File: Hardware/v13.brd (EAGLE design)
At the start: 50 x 50 mm, 86 parts, among them J1 22-27-2081-08, J2 22-27-2031-03

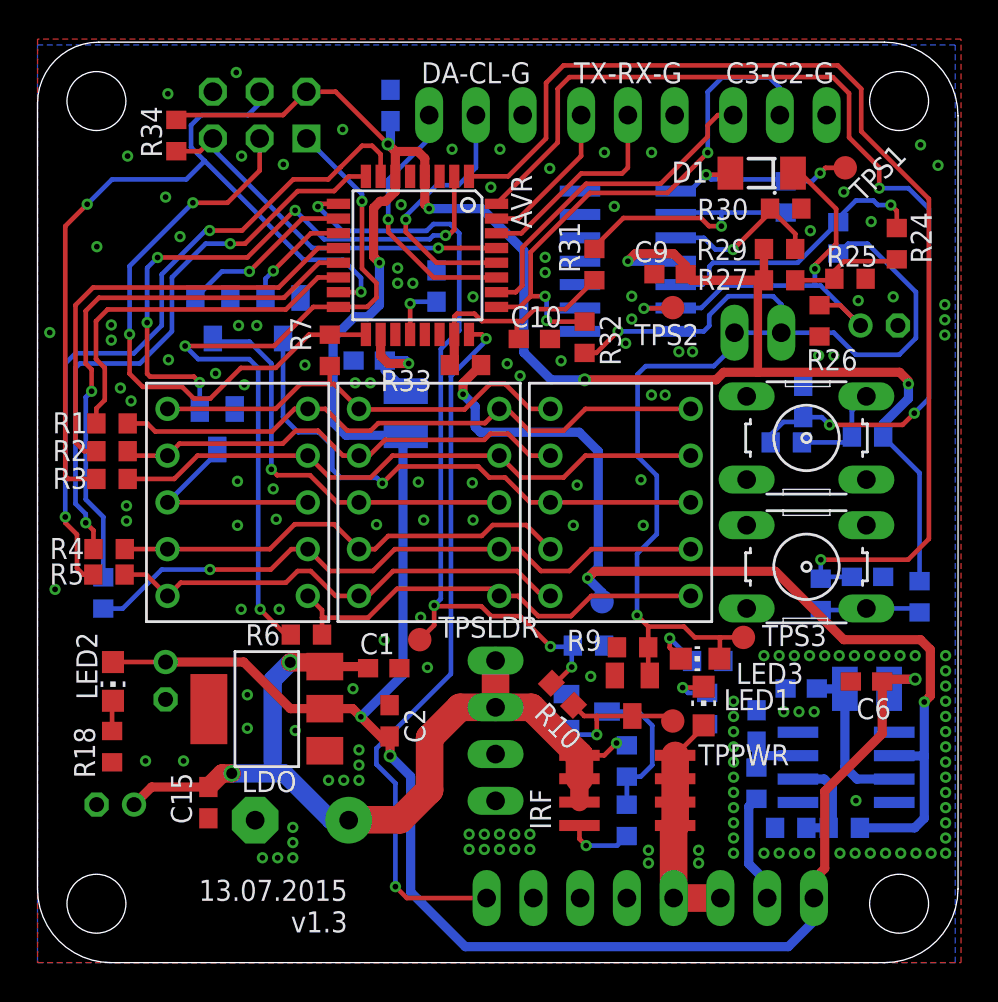
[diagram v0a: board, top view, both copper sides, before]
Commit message: added 5v pin header for twi added optional pull-ups for twi moved some parts around and rerouted some wires
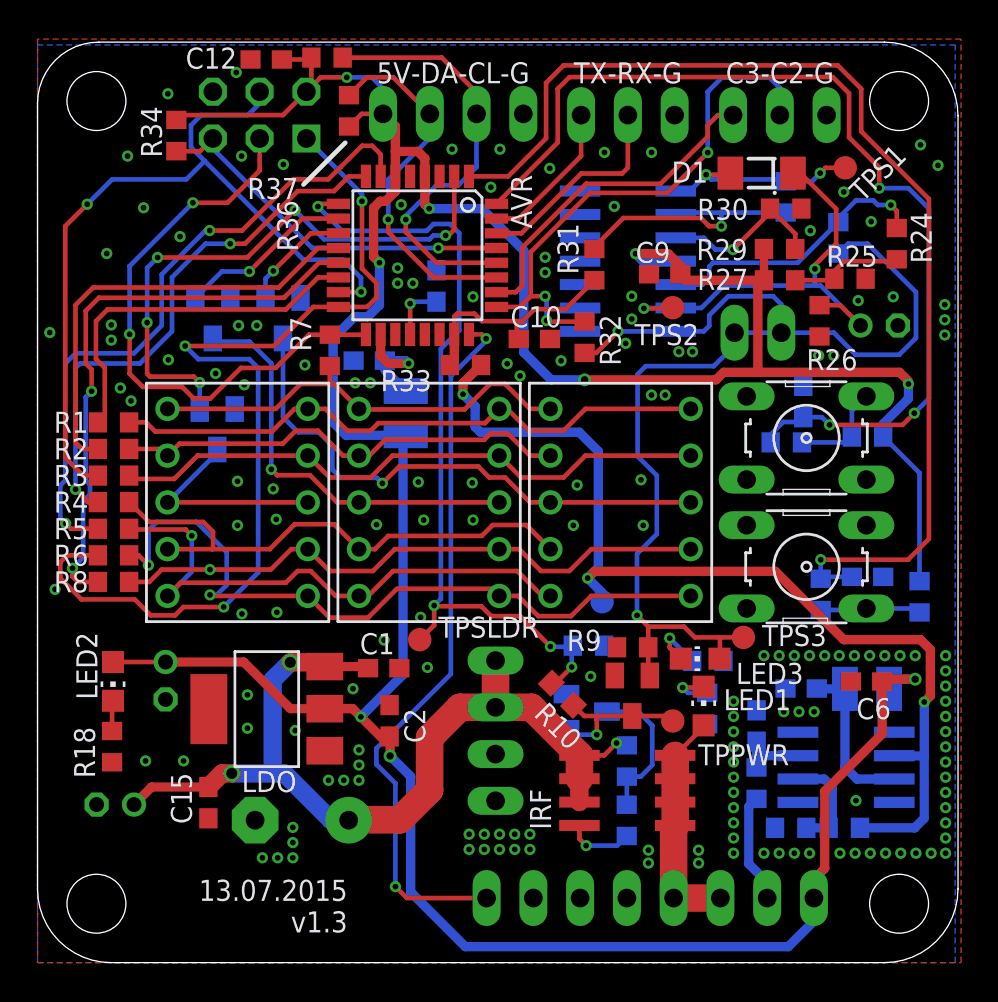
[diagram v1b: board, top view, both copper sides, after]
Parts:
- added R36, R37: 4k7, rcl:R0603
- I2C: value 22-27-2031-03 -> 22-27-2041-04; device con-molex:6410-03 -> con-molex:6410-04
- R25: value 6.2k -> 6k2
- moved R6 11.3 mm to (4.13, 22.1)
- moved C12 7.20 mm to (12.4, 49.1), flipped to the top, turned to 180 degrees
- moved R4 2.56 mm to (4.13, 25.0)
- moved R5 2.50 mm to (4.13, 23.6)
- moved I2C 1.24 mm to (22.6, 46.1)
- moved R8 0.82 mm to (4.13, 20.7), flipped to the top, turned to 180 degrees
- moved C9 0.29 mm to (34.1, 37.4)
- moved R3 0.20 mm to (4.13, 26.5)
- moved R2 0.14 mm to (4.13, 27.9)
- moved R1 0.10 mm to (4.13, 29.3)
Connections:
- net GND: now also I2C.4; no longer I2C.3
- net SCL: now also I2C.3, R37.1; no longer I2C.2
- net SDA: now also I2C.2, R36.1; no longer I2C.1
- net VCC: now also I2C.1, R36.2, R37.2
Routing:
- net N$31: track 24.2 -> 39.6 mm, vias 0 -> 2
- net MISO: track 41.6 -> 52.9 mm
- net SCL: track 14.2 -> 23.5 mm
- net VCC: track 188.4 -> 194.3 mm
- net SDA: track 14.2 -> 19.9 mm
- net N$37: track 25.9 -> 30.4 mm, vias 0 -> 1
- net N$36: track 25.3 -> 29.2 mm
- net LCD_E: track 32.0 -> 29.9 mm
- net N$38: track 35.2 -> 33.2 mm
- net LCD_D: track 37.5 -> 35.8 mm
- net LCD_C: track 29.9 -> 31.5 mm, vias 1 -> 2
- net MOSI: track 44.6 -> 44.0 mm
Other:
- board text added: "5V-DA-CL-G"
- board text removed: "DA-CL-G"

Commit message: [hardware] Adds A4 frame to schematic, Signalnames
and changed name of signal of pwm output to PWM_OUT
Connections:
- net N$33 renamed PWM_OUT
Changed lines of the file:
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@@
 <?xml version="1.0" encoding="utf-8"?>
 <!DOCTYPE eagle SYSTEM "eagle.dtd">
-<eagle version="7.2.0">
+<eagle version="7.3.0">
 <drawing>
 <settings>
@@
 <wire x1="32.013525" y1="8.587475" x2="32.004" y2="8.57795" width="0.254" layer="16"/>
 </signal>
-<signal name="N$33">
+<signal name="PWM_OUT">
 <contactref element="IRF" pad="8"/>
 <contactref element="IRF" pad="7"/>

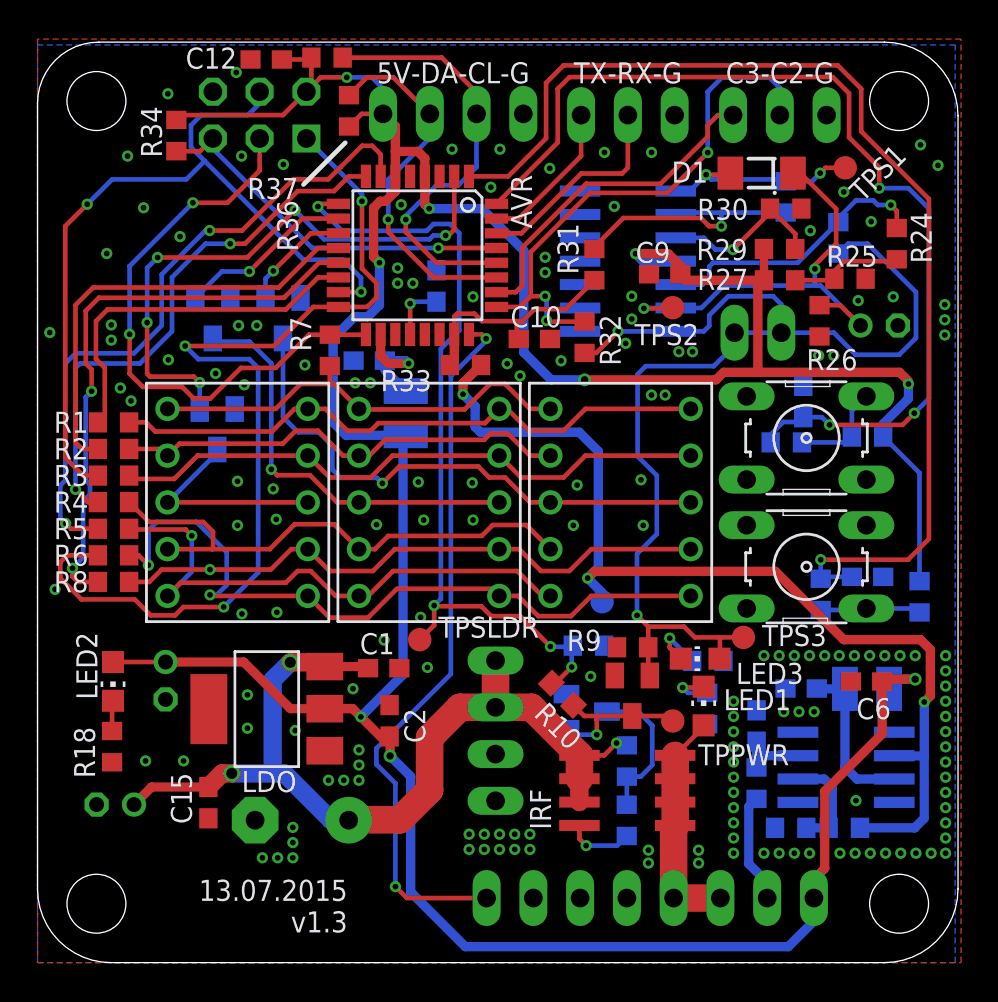
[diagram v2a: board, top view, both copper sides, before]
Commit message: changed radius of round corners changed location of the drilling holes slightly cleared some space around the drilling holes added 2x 10k to set all unused LM324 inputs to a 2,5V moved some components around
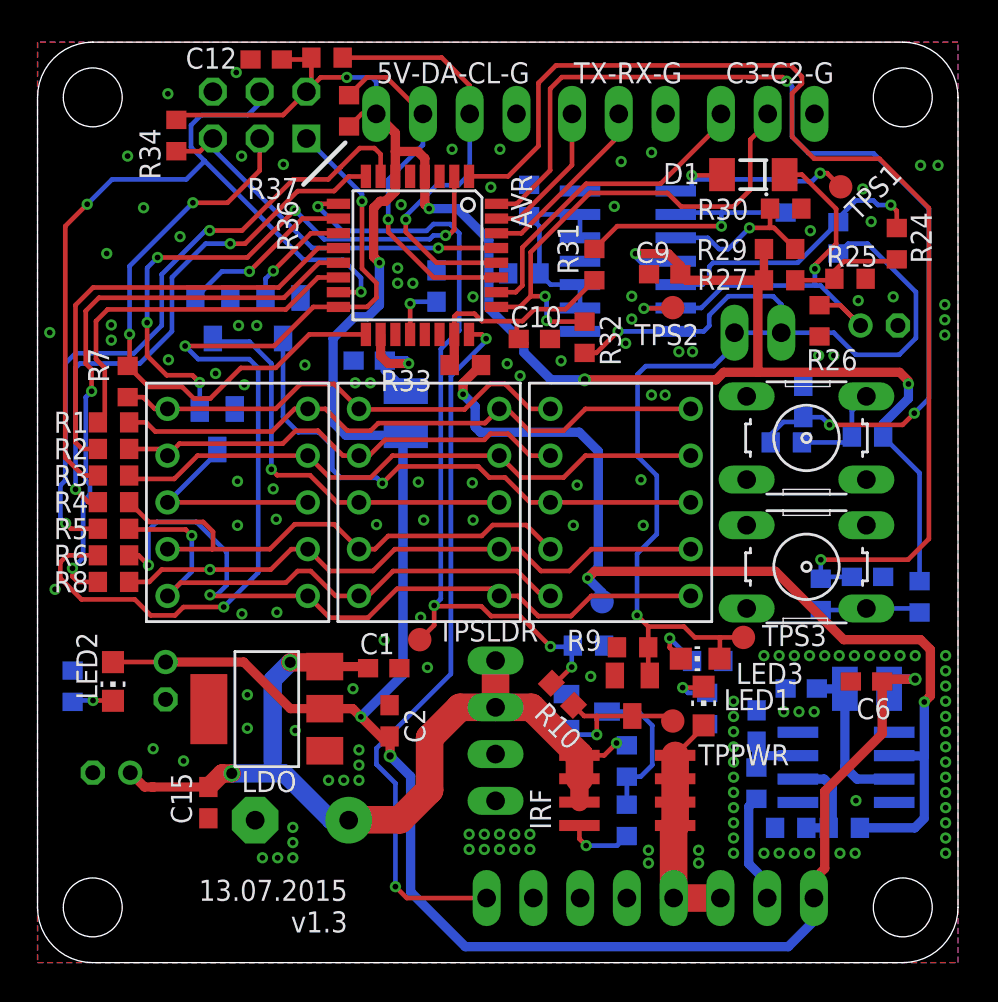
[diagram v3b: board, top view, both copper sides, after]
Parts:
- added R39, R40: 10k, rcl:R0603
- moved R7 11.1 mm to (4.90, 31.6)
- moved R18 3.92 mm to (1.91, 15.0), flipped to the bottom, turned to 270 degrees
- moved C14 1.75 mm to (4.02, 10.3)
- moved TPS1 1.06 mm to (43.6, 42.1)
- moved J2 0.66 mm to (39.7, 46.1)
- moved UART 0.50 mm to (31.6, 46.1)
- moved D1 0.46 mm to (38.9, 42.8)
- moved I2C 0.37 mm to (22.2, 46.1)
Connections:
- new net N$4: LM324.10, LM324.12, LM324.13, LM324.9, R39.2, R40.1
- net GND: now also R40.2
- net VCC: now also R39.1
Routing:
- net N$4: track 0.00 -> 11.1 mm
- net PC2: track 30.3 -> 27.6 mm, vias 3 -> 2
- net RX: track 11.5 -> 10.0 mm
- net N$35: track 24.1 -> 25.5 mm
- net BUTTON_+: track 61.2 -> 62.4 mm
- net PC3: track 18.4 -> 17.7 mm
- net N$7: track 11.4 -> 12.0 mm
- net N$24: track 1.66 -> 2.23 mm, vias 0 -> 1
- net SDA: track 19.9 -> 19.3 mm
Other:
- outline, holes or cut-outs redrawn

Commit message: changed arrangement of parts to be almost all vertical
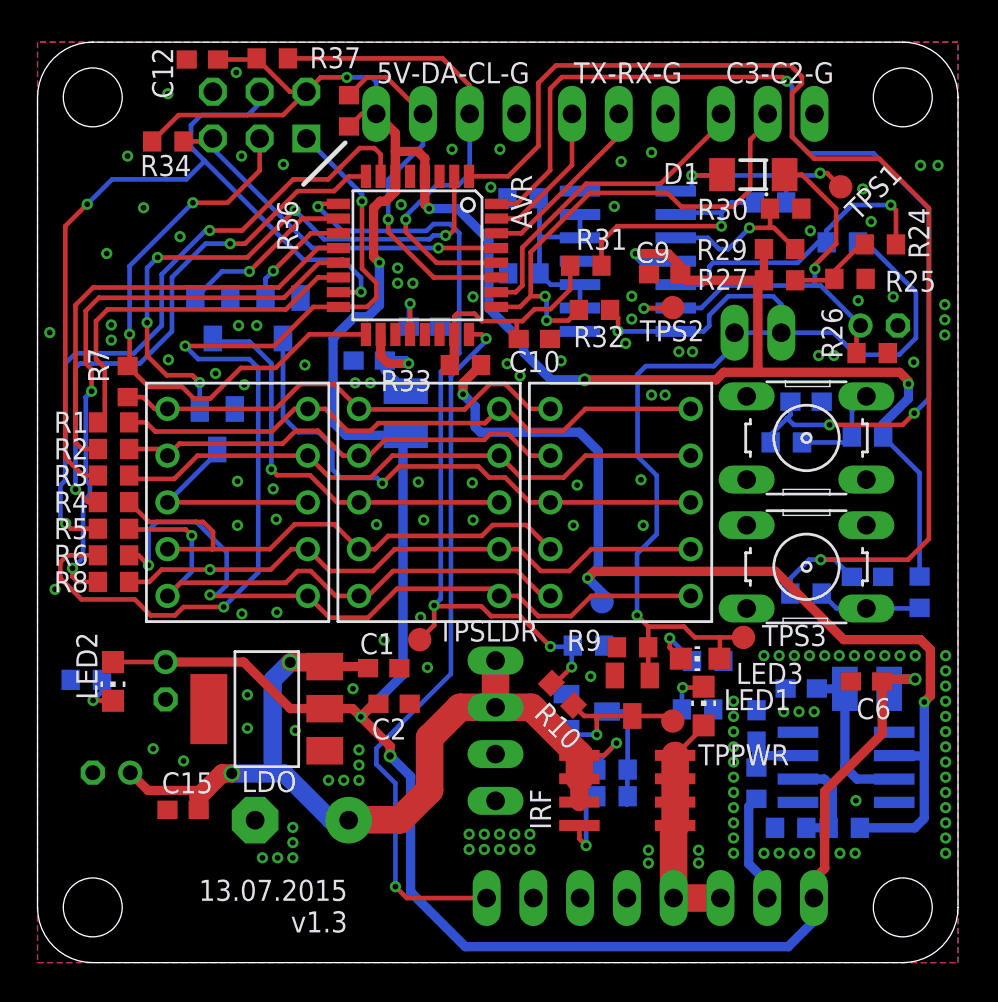
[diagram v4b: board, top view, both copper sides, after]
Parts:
- moved C12 3.47 mm to (8.95, 49.1)
- moved R26 3.35 mm to (45.3, 33.1), turned to 0 degrees
- moved R37 2.97 mm to (12.8, 49.1)
- moved C17 2.30 mm to (21.0, 34.5), turned to 0 degrees
- moved R32 1.58 mm to (30.3, 35.5), turned to 180 degrees
- moved R14 1.54 mm to (31.2, 9.04), turned to 180 degrees
- moved C15 1.43 mm to (7.91, 8.30), turned to 0 degrees
- moved C2 0.96 mm to (19.4, 14.1), turned to 180 degrees
- moved R15 0.94 mm to (31.2, 10.5), turned to 0 degrees
- moved R24 0.89 mm to (45.8, 39.0), turned to 180 degrees
- moved R35 0.88 mm to (39.8, 41.3), turned to 0 degrees
- moved R18 0.82 mm to (2.65, 15.4), turned to 180 degrees
- moved R21 0.80 mm to (41.7, 20.1), turned to 0 degrees
- moved R34 0.56 mm to (7.08, 44.6), turned to 0 degrees
- moved R11 0.52 mm to (35.9, 13.8), turned to 0 degrees
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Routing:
- net VCC: track 194.2 -> 198.9 mm
- net SCL: track 23.2 -> 26.2 mm
- net 12V: track 50.4 -> 53.1 mm
- net SAFETY: track 63.8 -> 61.3 mm
- net BUTTON_+: track 62.4 -> 64.6 mm
- net N$14: track 6.23 -> 4.82 mm
- net N$7: track 12.0 -> 13.3 mm
- net P-FET_GATE: track 8.10 -> 6.86 mm
- net N$11: track 25.7 -> 24.6 mm
- net BUTTON_-: track 54.0 -> 54.9 mm
- net N$12: track 15.6 -> 16.5 mm
- net N$6: track 14.3 -> 13.5 mm
- net RST: track 20.5 -> 19.9 mm
